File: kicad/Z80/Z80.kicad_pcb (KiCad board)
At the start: 2 copper layers, 43.2 x 58.4 mm, 26 parts, among them J1 Conn_01x02, SW1 SW_DIP_x01, U1 HEF4093B, U2 Z80CPU

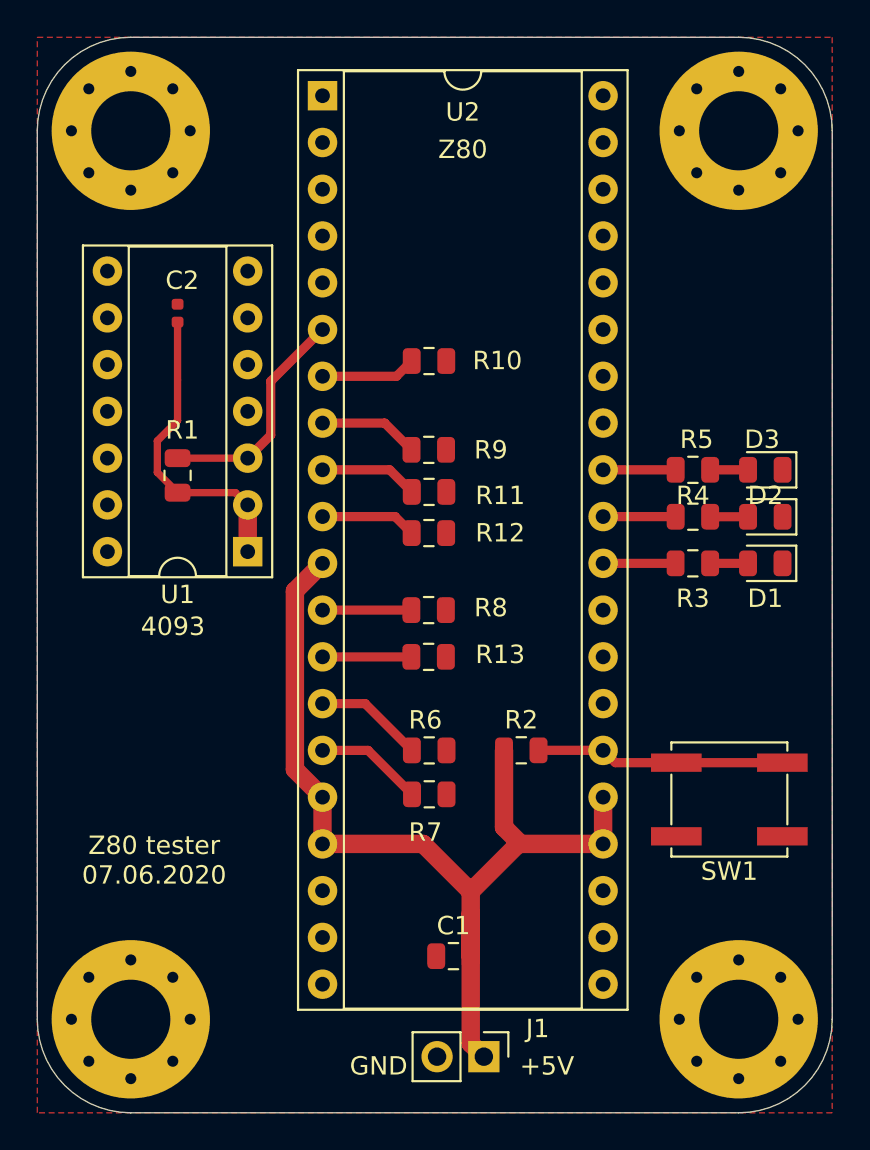
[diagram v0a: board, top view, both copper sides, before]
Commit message: add FPGA
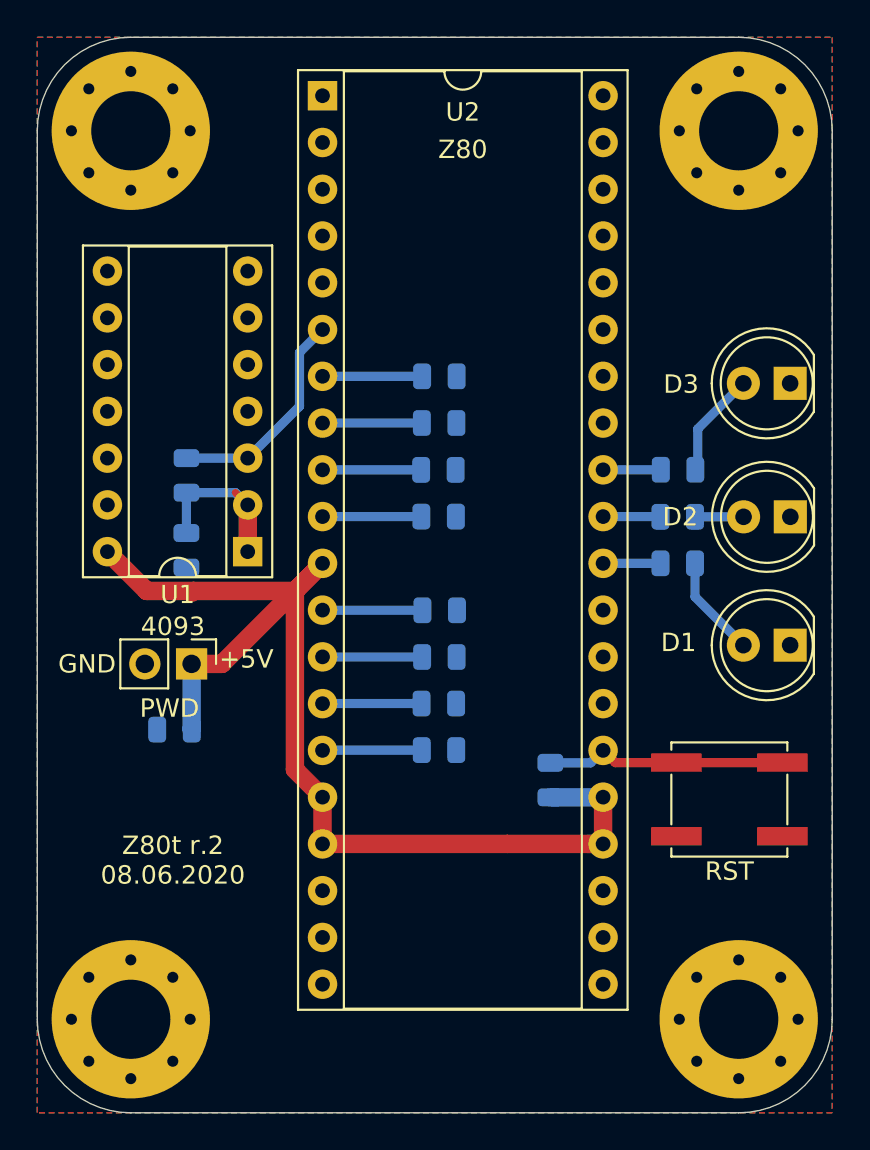
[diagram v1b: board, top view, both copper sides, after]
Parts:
- C1, R1, R10, R11, R12, R13, R2, R3, R4, R5, R6, R7, R8, R9: moved to B.Cu
- C2: footprint Capacitor_SMD:C_0402_1005Metric -> Capacitor_SMD:C_0805_2012Metric; moved to B.Cu
- D1, D2, D3: footprint LED_SMD:LED_0805_2012Metric -> LED_THT:LED_D5.0mm_Clear
- PWD: renamed from J1; value Conn_01x02 -> 01x02
- moved PWD 26.6 mm to (47.8, 72.1)
- moved C1 19.5 mm to (46.8, 75.7)
- moved C2 12.9 mm to (47.5, 66.0), turned to 270 degrees
- moved D3 4.89 mm to (80.3, 56.9)
- moved D1 4.65 mm to (80.3, 71.1)
- moved R6 2.60 mm to (61.2, 74.3)
- moved R7 2.46 mm to (61.2, 76.8)
- moved R2 2.26 mm to (67.2, 78.4), turned to 90 degrees
- moved R9 1.56 mm to (61.2, 59.1)
- moved D2 1.36 mm to (80.3, 64.1)
- moved R11 1.30 mm to (61.2, 61.6)
- moved R12 1.04 mm to (61.2, 64.1)
- moved R10 1.00 mm to (61.2, 56.5)
- moved R4 0.83 mm to (74.2, 64.1)
- moved R3 0.82 mm to (74.2, 66.7)
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- renumbered SW1 to RST
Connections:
- U1 pad 14: (no net) -> VCC
- U1 pad 7: (no net) -> GND
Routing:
- net VCC: track 53.5 -> 62.1 mm
- net Net-(C2-Pad1): track 16.8 -> 9.28 mm
- net Net-(D3-Pad2): track 2.11 -> 5.73 mm
- net Net-(D1-Pad2): track 2.06 -> 5.53 mm
- net Net-(D2-Pad2): track 2.06 -> 3.03 mm
- net Net-(R3-Pad1): track 3.94 -> 3.12 mm
- net Net-(R4-Pad1): track 3.89 -> 3.13 mm
- net Net-(R5-Pad1): track 3.89 -> 3.27 mm
- net Net-(R8-Pad1): track 4.83 -> 5.43 mm
- net Net-(R13-Pad1): track 4.83 -> 5.41 mm
- net Net-(R6-Pad1): track 5.91 -> 5.38 mm
- added copper zone on B.Cu, net GND
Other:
- board text added: "+"
- board text added: "Z80t r.2 08.06.2020"
- board text removed: "Z80 tester 07.06.2020"

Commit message: Генератор курсовых работ
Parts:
- added C3: 1uF, Capacitor_SMD:C_0805_2012Metric, B.Cu at (61.2, 66.7)
- added C4: 100nF, Capacitor_SMD:C_0805_2012Metric, B.Cu at (45.4, 66.0)
- added D4: POWER, LED_SMD:LED_1206_3216Metric, F.Cu at (44.3, 76.4)
- added R14: 470, Resistor_SMD:R_0805_2012Metric, F.Cu at (47.7, 75.9)
- C1: value 100nf -> 100nF
- C2: value 1u -> 1uF
- renumbered PWD to J1, RST to SW1
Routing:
- net VCC: track 62.1 -> 73.1 mm
- net Net-(D4-Pad2): track 0.00 -> 2.17 mm
- net GND: vias 0 -> 35
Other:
- board text added: "Z80T r.3 01.07.2020"
- board text removed: "Z80t r.2 08.06.2020"
